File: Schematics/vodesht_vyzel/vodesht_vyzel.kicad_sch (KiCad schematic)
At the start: 3 parts, among them U1 SSD1306, U2 NODEMCU32S, U3 NRF52840-DONGLE

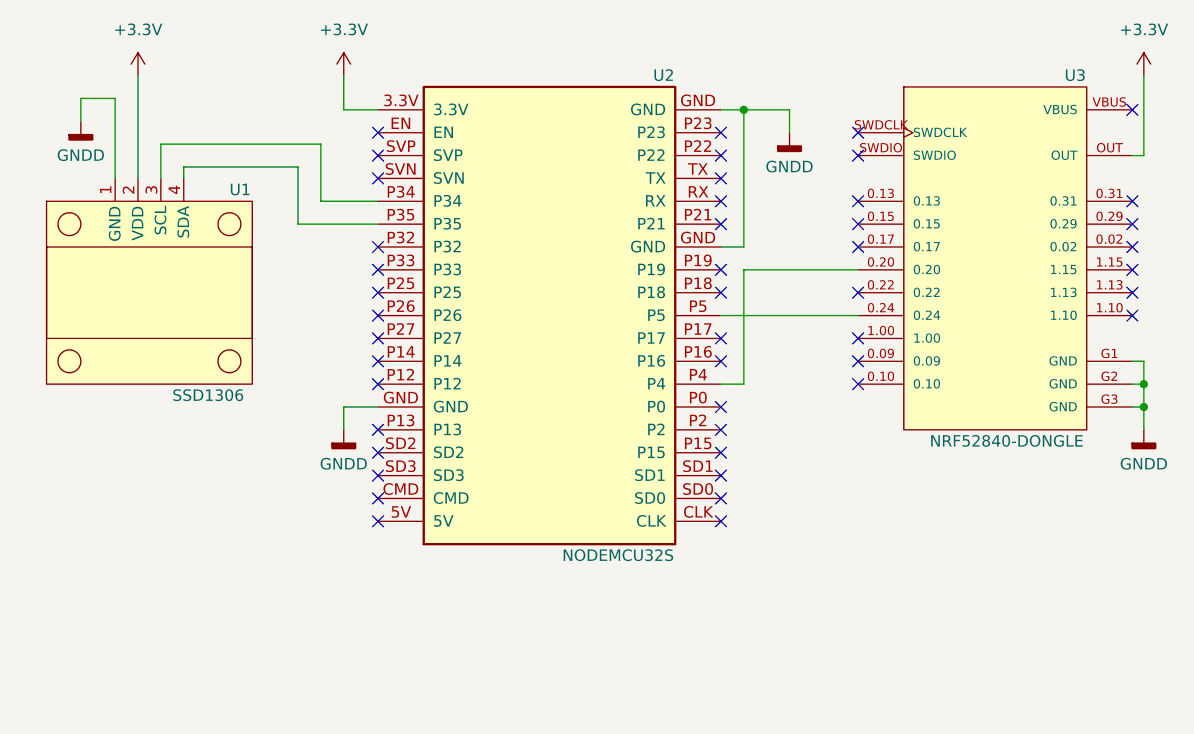
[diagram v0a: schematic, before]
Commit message: Edited the pcb board of the vodesht_vyzel and did some small changes on the pcb of the main module
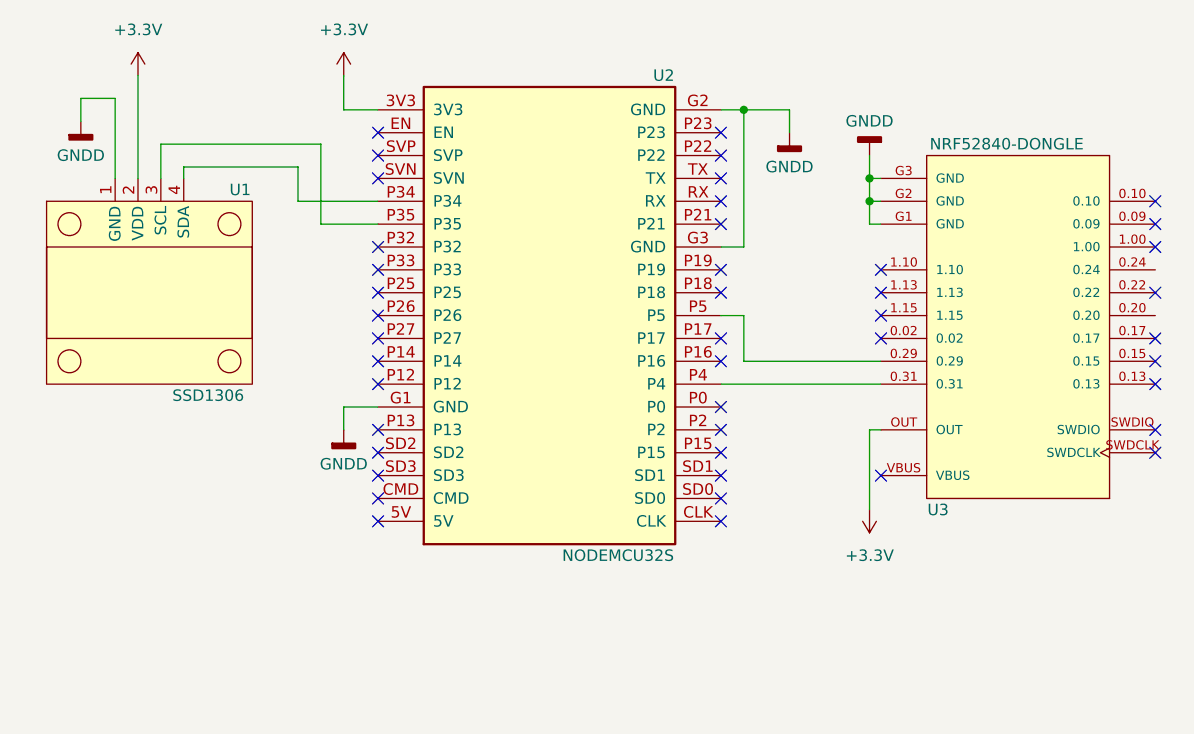
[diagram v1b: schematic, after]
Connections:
- net +3.3V: now also U2.3V3; no longer U2.3.3V
- net GNDD: now also U2.G1 (GND), U2.G2 (GND), U2.G3 (GND); no longer U2.GND
- net at U3.0.20: no longer U2.P4
- net at U3.0.24: no longer U2.P5
- net at U3.0.29: now also U2.P5
- net at U3.0.31: now also U2.P4
- net at U1.3 (SCL): now also U2.P35; no longer U2.P34
- net at U1.4 (SDA): now also U2.P34; no longer U2.P35
- no-connect marks 46 -> 44
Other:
- moved on the sheet: U3

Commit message: Fixed some footprints and made changes on the leader node pcb
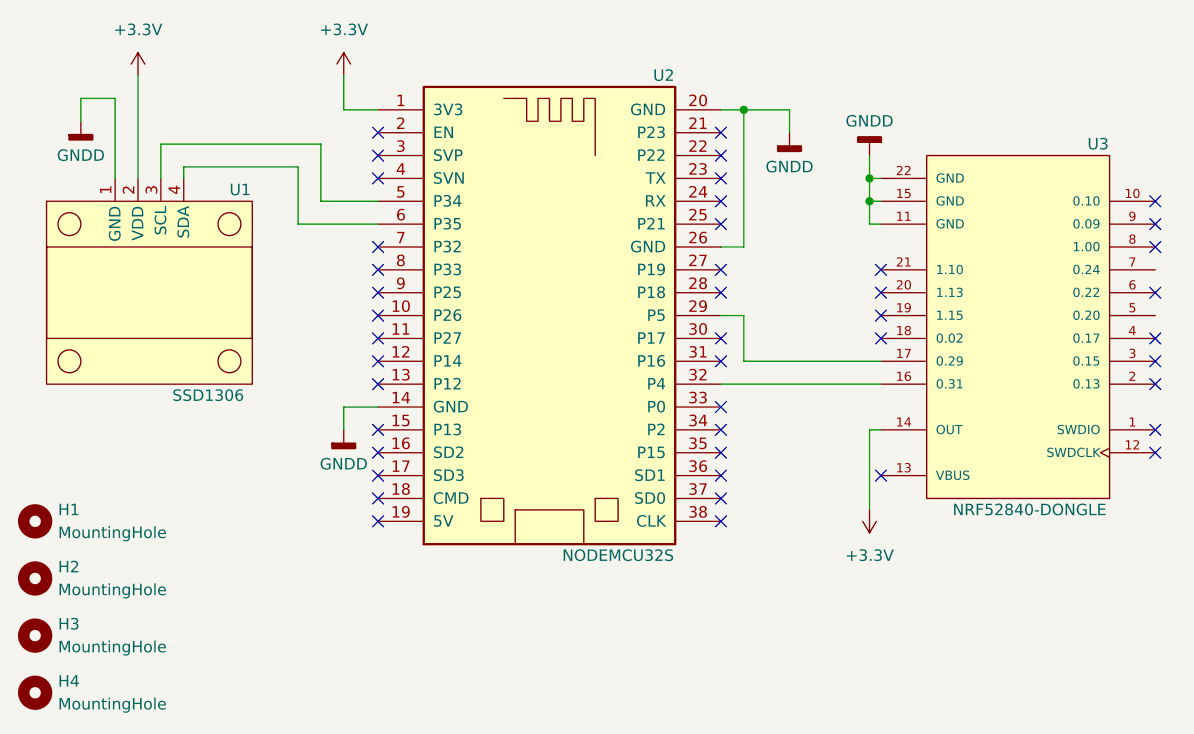
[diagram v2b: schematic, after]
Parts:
- added H1, H2, H3, H4: MountingHole, MountingHole:MountingHole_2.5mm, symbol Mechanical:MountingHole
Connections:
- net +3.3V: now also U2.1 (3V3), U3.14 (OUT); no longer U2.3V3, U3.OUT
- net GNDD: now also U2.14 (GND), U2.20 (GND), U2.26 (GND), U3.11 (GND), U3.15 (GND), U3.22 (GND); no longer U2.G1 (GND), U2.G2 (GND), U2.G3 (GND), U3.G1 (GND), U3.G2 (GND), U3.G3 (GND)
- net at U1.3 (SCL): now also U2.5 (P34); no longer U2.P35
- net at U1.4 (SDA): now also U2.6 (P35); no longer U2.P34
- new net: U2.32 (P4), U3.16 (0.31)
- new net: U2.29 (P5), U3.17 (0.29)

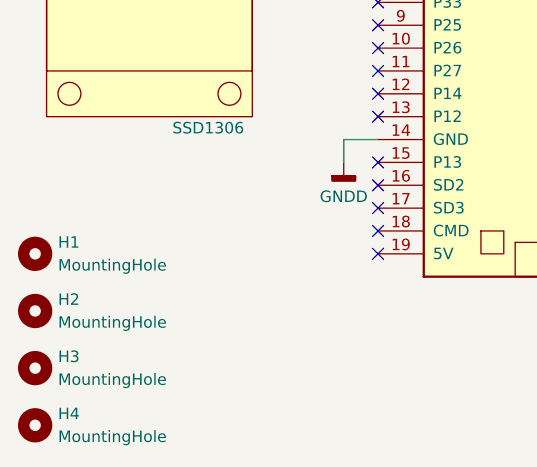
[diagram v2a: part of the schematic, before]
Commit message: Made small changes in the schematics
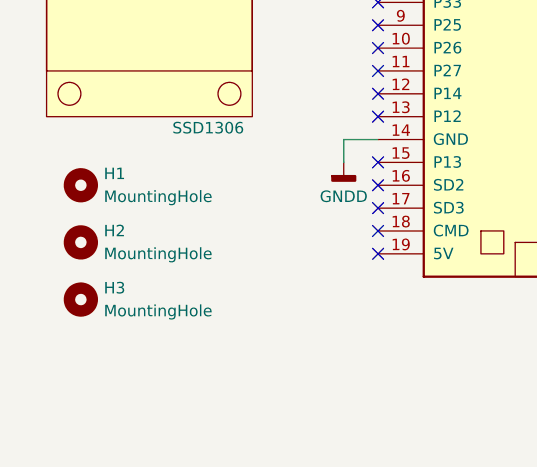
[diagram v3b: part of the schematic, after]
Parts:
- removed H4: MountingHole, MountingHole:MountingHole_2.5mm, symbol Mechanical:MountingHole
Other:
- moved on the sheet: H1, H2, H3
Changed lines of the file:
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@@
     (pin "1")
   )
-  (symbol (lib_id "Mechanical:MountingHole") (at 83.82 114.3 0) (unit 1)
-    (in_bom yes) (on_board yes) (fields_autoplaced)
-    (property "Reference" "H1" (id 0) (at 86.36 113.0299 0)
-      (effects (font (size 1.27 1.27)) (justify left))
-    )
-    (property "Value" "MountingHole" (id 1) (at 86.36 115.5699 0)
-      (effects (font (size 1.27 1.27)) (justify left))
-    )
-    (property "Footprint" "MountingHole:MountingHole_2.5mm" (id 2) (at 83.82 114.3 0)
-      (effects (font (size 1.27 1.27)) hide)
-    )
-    (property "Datasheet" "~" (id 3) (at 83.82 114.3 0)
+  (symbol (lib_id "Mechanical:MountingHole") (at 88.9 106.68 0) (unit 1)
+    (in_bom yes) (on_board yes) (fields_autoplaced)
+    (property "Reference" "H1" (id 0) (at 91.44 105.4099 0)
+      (effects (font (size 1.27 1.27)) (justify left))
+    )
+    (property "Value" "MountingHole" (id 1) (at 91.44 107.9499 0)
+      (effects (font (size 1.27 1.27)) (justify left))
+    )
+    (property "Footprint" "MountingHole:MountingHole_2.5mm" (id 2) (at 88.9 106.68 0)
+      (effects (font (size 1.27 1.27)) hide)
+    )
+    (property "Datasheet" "~" (id 3) (at 88.9 106.68 0)
       (effects (font (size 1.27 1.27)) hide)
     )
@@
     (pin "9")
   )
-  (symbol (lib_id "Mechanical:MountingHole") (at 83.82 133.35 0) (unit 1)
-    (in_bom yes) (on_board yes) (fields_autoplaced)
-    (property "Reference" "H4" (id 0) (at 86.36 132.0799 0)
-      (effects (font (size 1.27 1.27)) (justify left))
-    )
-    (property "Value" "MountingHole" (id 1) (at 86.36 134.6199 0)
-      (effects (font (size 1.27 1.27)) (justify left))
-    )
-    (property "Footprint" "MountingHole:MountingHole_2.5mm" (id 2) (at 83.82 133.35 0)
-      (effects (font (size 1.27 1.27)) hide)
-    )
-    (property "Datasheet" "~" (id 3) (at 83.82 133.35 0)
-      (effects (font (size 1.27 1.27)) hide)
-    )
-  )
   (symbol (lib_id "power:+3.3V") (at 176.53 113.03 180) (unit 1)
     (in_bom yes) (on_board yes) (fields_autoplaced)
@@
     (pin "1")
   )
-  (symbol (lib_id "Mechanical:MountingHole") (at 83.82 127 0) (unit 1)
-    (in_bom yes) (on_board yes) (fields_autoplaced)
-    (property "Reference" "H3" (id 0) (at 86.36 125.7299 0)
-      (effects (font (size 1.27 1.27)) (justify left))
-    )
-    (property "Value" "MountingHole" (id 1) (at 86.36 128.2699 0)
-      (effects (font (size 1.27 1.27)) (justify left))
-    )
-    (property "Footprint" "MountingHole:MountingHole_2.5mm" (id 2) (at 83.82 127 0)
-      (effects (font (size 1.27 1.27)) hide)
-    )
-    (property "Datasheet" "~" (id 3) (at 83.82 127 0)
+  (symbol (lib_id "Mechanical:MountingHole") (at 88.9 119.38 0) (unit 1)
+    (in_bom yes) (on_board yes) (fields_autoplaced)
+    (property "Reference" "H3" (id 0) (at 91.44 118.1099 0)
+      (effects (font (size 1.27 1.27)) (justify left))
+    )
+    (property "Value" "MountingHole" (id 1) (at 91.44 120.6499 0)
+      (effects (font (size 1.27 1.27)) (justify left))
+    )
+    (property "Footprint" "MountingHole:MountingHole_2.5mm" (id 2) (at 88.9 119.38 0)
+      (effects (font (size 1.27 1.27)) hide)
+    )
+    (property "Datasheet" "~" (id 3) (at 88.9 119.38 0)
       (effects (font (size 1.27 1.27)) hide)
     )
@@
     (pin "4")
   )
-  (symbol (lib_id "Mechanical:MountingHole") (at 83.82 120.65 0) (unit 1)
-    (in_bom yes) (on_board yes) (fields_autoplaced)
-    (property "Reference" "H2" (id 0) (at 86.36 119.3799 0)
-      (effects (font (size 1.27 1.27)) (justify left))
-    )
-    (property "Value" "MountingHole" (id 1) (at 86.36 121.9199 0)
-      (effects (font (size 1.27 1.27)) (justify left))
-    )
-    (property "Footprint" "MountingHole:MountingHole_2.5mm" (id 2) (at 83.82 120.65 0)
-      (effects (font (size 1.27 1.27)) hide)
-    )
-    (property "Datasheet" "~" (id 3) (at 83.82 120.65 0)
+  (symbol (lib_id "Mechanical:MountingHole") (at 88.9 113.03 0) (unit 1)
+    (in_bom yes) (on_board yes) (fields_autoplaced)
+    (property "Reference" "H2" (id 0) (at 91.44 111.7599 0)
+      (effects (font (size 1.27 1.27)) (justify left))
+    )
+    (property "Value" "MountingHole" (id 1) (at 91.44 114.2999 0)
+      (effects (font (size 1.27 1.27)) (justify left))
+    )
+    (property "Footprint" "MountingHole:MountingHole_2.5mm" (id 2) (at 88.9 113.03 0)
+      (effects (font (size 1.27 1.27)) hide)
+    )
+    (property "Datasheet" "~" (id 3) (at 88.9 113.03 0)
       (effects (font (size 1.27 1.27)) hide)
     )
@@
       (reference "H3") (unit 1) (value "MountingHole") (footprint "MountingHole:MountingHole_2.5mm")
     )
-    (path "/82d35475-d3d6-4313-8406-4eafaa575977"
-      (reference "H4") (unit 1) (value "MountingHole") (footprint "MountingHole:MountingHole_2.5mm")
-    )
     (path "/df6f0d16-7cfe-4908-9644-8b61fb6f2a89"

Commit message: Generated new gerber files for the leader_node pcb
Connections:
- net at U1.3 (SCL): now also U2.7 (P32); no longer U2.5 (P34)
- net at U1.4 (SDA): now also U2.8 (P33); no longer U2.6 (P35)
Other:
- moved on the sheet: U3
